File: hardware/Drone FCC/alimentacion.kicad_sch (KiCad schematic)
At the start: 20 parts, among them J901 PM02 PixHawk, Q901 Q_PMOS_GSD, U901 ZLDO1117QG33TA

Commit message: routing: connected everything
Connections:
- net 5V: now also C903.1, D902.1 (K), D903.1 (K), U901.3 (VI); no longer D903.2 (A), J901.1, J901.2
- net 5Vin: now also D903.2 (A), J901.1, J901.2; no longer C903.1, D902.1 (K), D903.1 (K), U901.3 (VI)
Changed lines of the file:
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@@
   (junction (at 42.545 133.35) (diameter 0) (color 0 0 0 0)
   )
+  (junction (at 174.625 36.195) (diameter 0) (color 0 0 0 0)
+  )
   (junction (at 167.64 36.195) (diameter 0) (color 0 0 0 0)
   )
@@
     (stroke (width 0) (type default) (color 0 0 0 0))
   )
-  (wire (pts (xy 167.64 36.195) (xy 182.245 36.195))
+  (wire (pts (xy 167.64 36.195) (xy 174.625 36.195))
     (stroke (width 0) (type default) (color 0 0 0 0))
   )
@@
     (stroke (width 0) (type default) (color 0 0 0 0))
   )
-  (wire (pts (xy 55.88 98.425) (xy 59.055 98.425))
+  (wire (pts (xy 55.88 98.425) (xy 60.325 98.425))
     (stroke (width 0) (type default) (color 0 0 0 0))
   )
@@
     (stroke (width 0) (type default) (color 0 0 0 0))
   )
+  (wire (pts (xy 174.625 27.305) (xy 174.625 36.195))
+    (stroke (width 0) (type default) (color 0 0 0 0))
+  )
   (wire (pts (xy 79.375 104.14) (xy 79.375 120.65))
     (stroke (width 0) (type default) (color 0 0 0 0))
@@
     (stroke (width 0) (type default) (color 0 0 0 0))
   )
+  (wire (pts (xy 179.705 27.305) (xy 174.625 27.305))
+    (stroke (width 0) (type default) (color 0 0 0 0))
+  )
   (wire (pts (xy 85.725 54.61) (xy 62.865 54.61))
     (stroke (width 0) (type default) (color 0 0 0 0))
@@
   )
   (wire (pts (xy 139.065 26.035) (xy 149.86 26.035))
+    (stroke (width 0) (type default) (color 0 0 0 0))
+  )
+  (wire (pts (xy 174.625 36.195) (xy 182.245 36.195))
     (stroke (width 0) (type default) (color 0 0 0 0))
   )
@@
     (effects (font (size 1.27 1.27)) (justify left bottom))
   )
-  (label "5Vin" (at 171.45 36.195 0)
-    (effects (font (size 1.27 1.27)) (justify left bottom))
-  )
-  (global_label "5V" (shape input) (at 137.795 52.07 180) (fields_autoplaced)
-    (effects (font (size 1.27 1.27)) (justify right))
-    (property "Intersheet References" "${INTERSHEET_REFS}" (id 0) (at 133.0838 52.1494 0)
-      (effects (font (size 1.27 1.27)) (justify right) hide)
-    )
+  (label "5Vin" (at 137.795 52.07 0)
+    (effects (font (size 1.27 1.27)) (justify left bottom))
+  )
+  (label "5Vin" (at 60.325 98.425 180)
+    (effects (font (size 1.27 1.27)) (justify right bottom))
   )
   (global_label "3V3" (shape input) (at 243.205 36.195 0) (fields_autoplaced)
@@
     )
   )
-  (global_label "5V" (shape input) (at 59.055 98.425 0) (fields_autoplaced)
+  (global_label "5V" (shape input) (at 179.705 27.305 0) (fields_autoplaced)
     (effects (font (size 1.27 1.27)) (justify left))
-    (property "Intersheet References" "${INTERSHEET_REFS}" (id 0) (at 63.7662 98.3456 0)
+    (property "Intersheet References" "${INTERSHEET_REFS}" (id 0) (at 184.4162 27.2256 0)
       (effects (font (size 1.27 1.27)) (justify left) hide)
     )

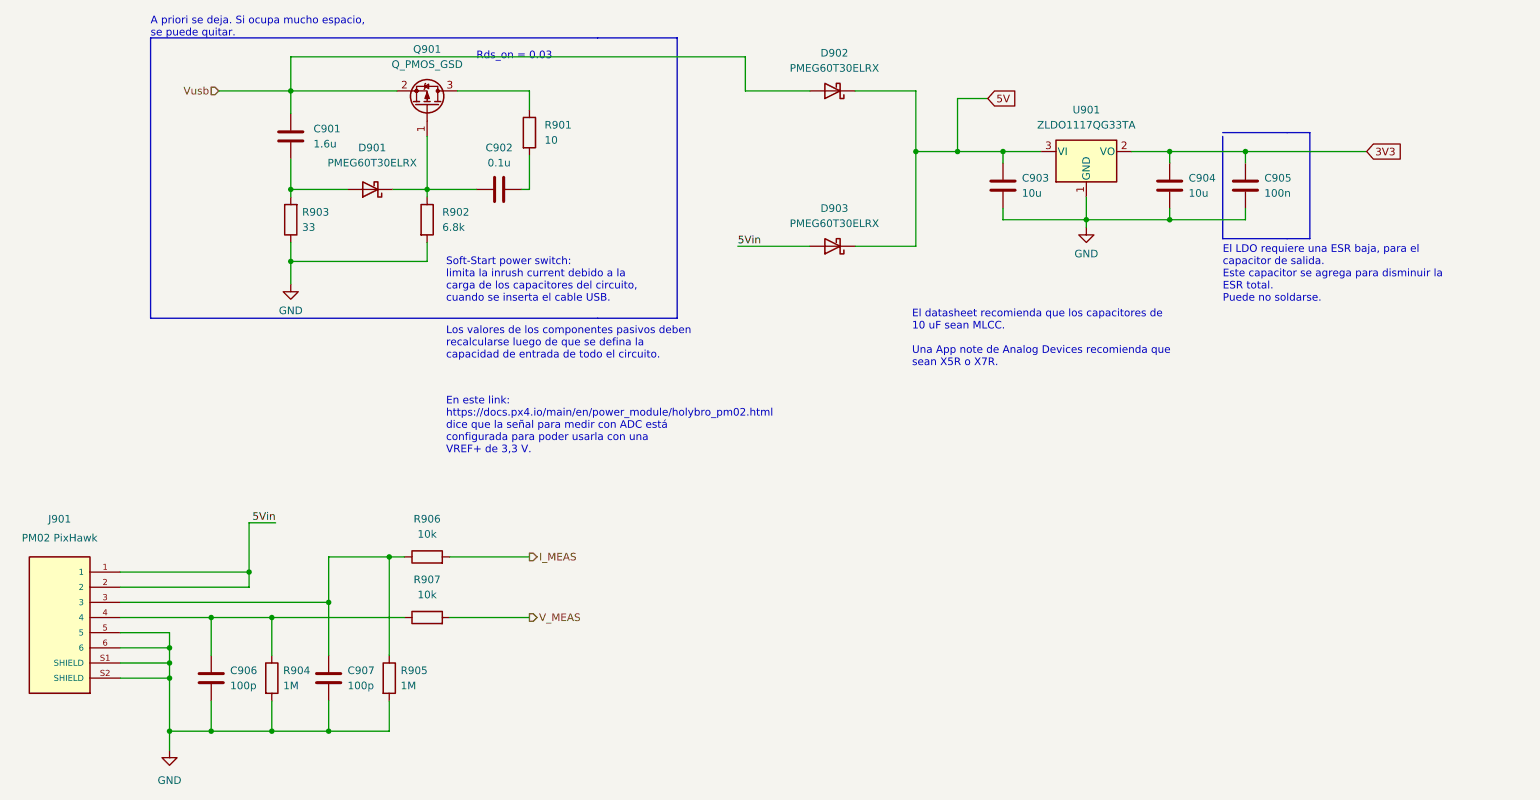
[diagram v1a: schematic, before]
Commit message: included all components on PCB
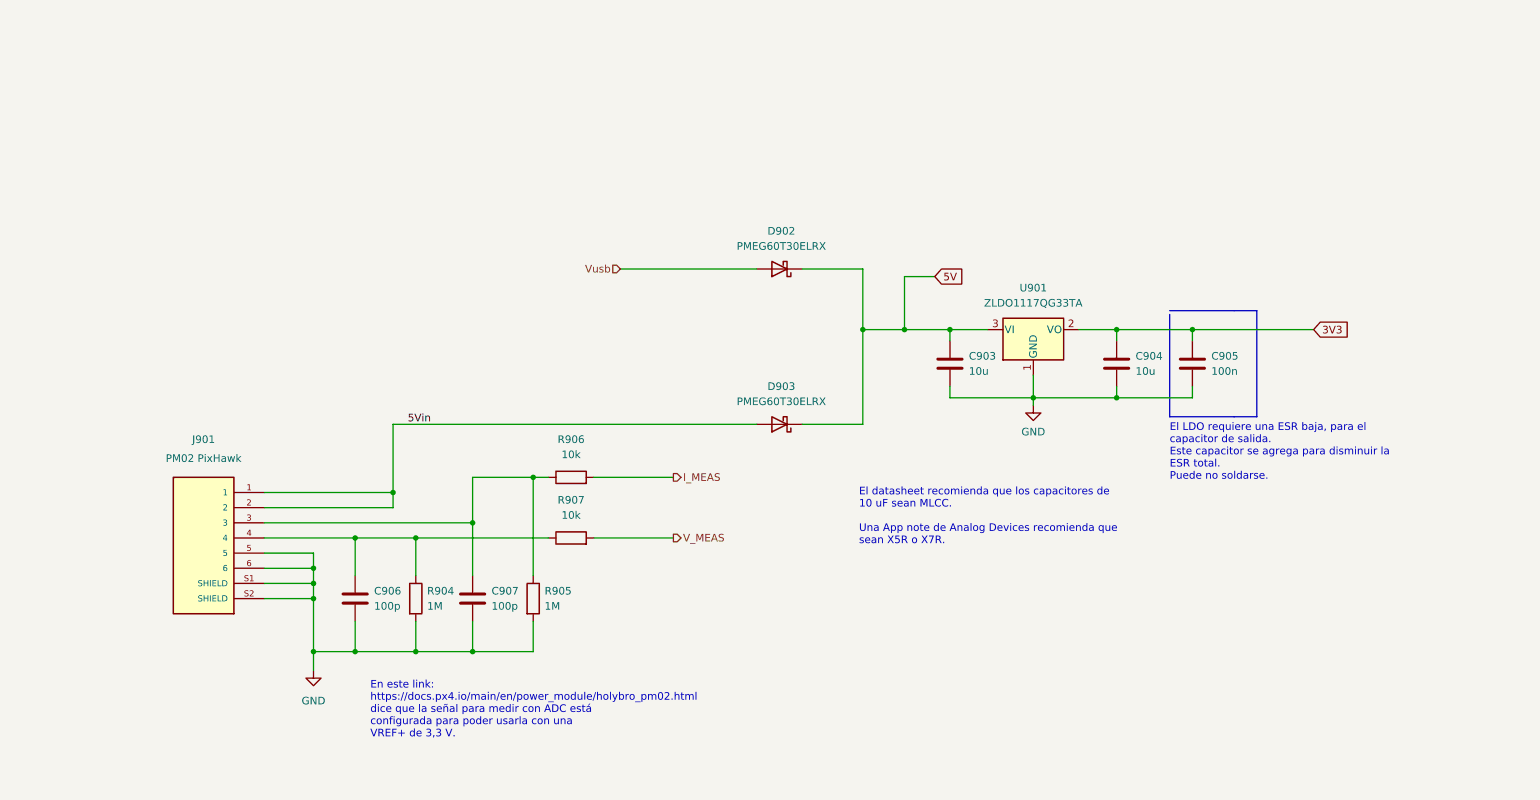
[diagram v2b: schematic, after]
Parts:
- removed C901: 1.6u, Capacitor_SMD:C_0603_1608Metric_Pad1.08x0.95mm_HandSolder, symbol Device:C
- removed C902: 0.1u, Capacitor_SMD:C_0603_1608Metric_Pad1.08x0.95mm_HandSolder, symbol Device:C
- removed D901: PMEG60T30ELRX, PMEG60T30ELRX:SODFL3517X110N, symbol Device:D_Schottky
- removed Q901: Q_PMOS_GSD, Package_TO_SOT_SMD:SOT-23, symbol Device:Q_PMOS_GSD
- removed R901: 10, Resistor_SMD:R_0603_1608Metric_Pad0.98x0.95mm_HandSolder, symbol Device:R
- removed R902: 6.8k, Resistor_SMD:R_0603_1608Metric_Pad0.98x0.95mm_HandSolder, symbol Device:R
- removed R903: 33, Resistor_SMD:R_0603_1608Metric_Pad0.98x0.95mm_HandSolder, symbol Device:R
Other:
- note removed: "A priori se deja. Si ocupa mucho espacio, se puede quitar."
- note removed: "Los valores de los componentes pasivos deben recalcularse luego de que se defina la capacidad de entrada de todo el circuito."
- note removed: "Rds_on = 0.03"
- note removed: "Soft-Start power switch: limita la inrush current debido a la carga de los capacitores del circuito, cuando se inserta el cable USB."
- moved on the sheet: C903, C904, C905, C906, C907, D902, D903, J901, R904, R905, R906, R907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

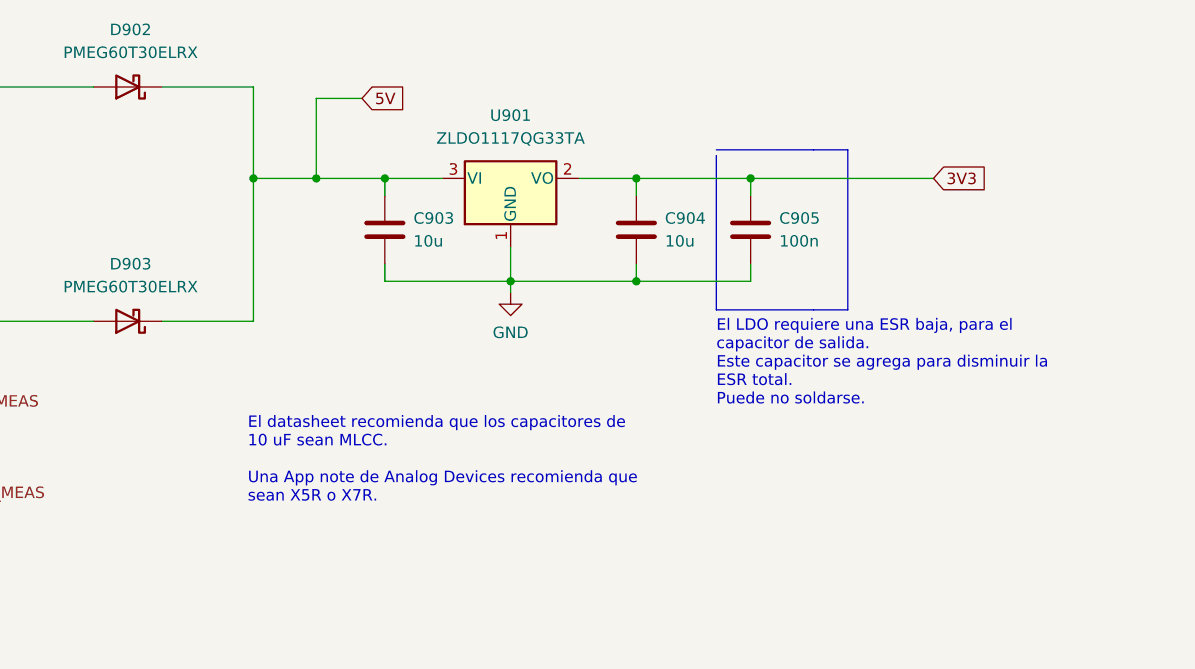
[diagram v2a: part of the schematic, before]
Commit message: LDO layout on PCB
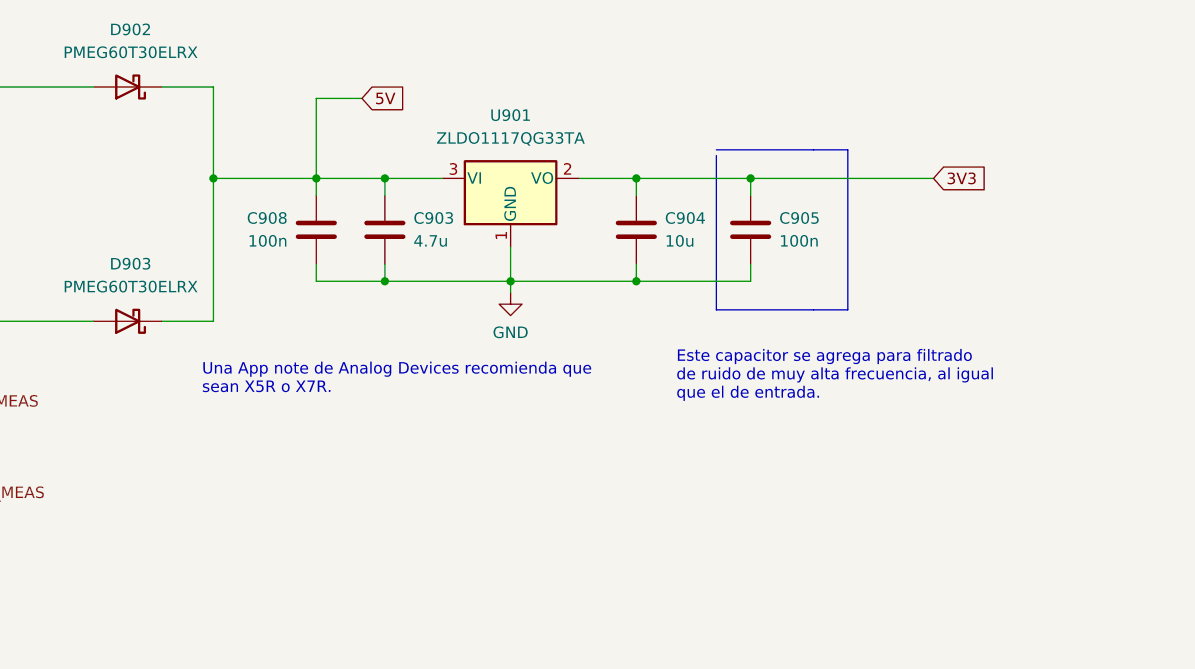
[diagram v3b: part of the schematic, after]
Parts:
- added C908: 100n, Capacitor_SMD:C_0603_1608Metric_Pad1.08x0.95mm_HandSolder, symbol Device:C
- C903: value 10u -> 4.7u; footprint Capacitor_SMD:C_0805_2012Metric_Pad1.18x1.45mm_HandSolder -> Capacitor_SMD:C_1206_3216Metric_Pad1.33x1.80mm_HandSolder
- C904: footprint Capacitor_SMD:C_0805_2012Metric_Pad1.18x1.45mm_HandSolder -> T491A106K016ATAUTO:CAPC3216X110N
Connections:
- net 5V: now also C908.2
- net GND: now also C908.1
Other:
- note added: "Este capacitor se agrega para filtrado de ruido de muy alta frecuencia, al igual que el de entrada."
- note added: "Una App note de Analog Devices recomienda que sean X5R o X7R."
- note removed: "El LDO requiere una ESR baja, para el capacitor de salida. Este capacitor se agrega para disminuir la ESR total. Puede no soldarse."
- note removed: "El datasheet recomienda que los capacitores de 10 uF sean MLCC. Una App note de Analog Devices recomienda que sean X5R o X7R."
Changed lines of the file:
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@@
   (junction (at 187.325 77.47) (diameter 0) (color 0 0 0 0)
   )
+  (junction (at 154.305 66.04) (diameter 0) (color 0 0 0 0)
+  )
   (junction (at 66.675 108.585) (diameter 0) (color 0 0 0 0)
   )
@@
   (junction (at 66.675 120.015) (diameter 0) (color 0 0 0 0)
   )
+  (junction (at 173.355 77.47) (diameter 0) (color 0 0 0 0)
+  )
   (junction (at 165.735 66.04) (diameter 0) (color 0 0 0 0)
   )
-  (junction (at 158.75 66.04) (diameter 0) (color 0 0 0 0)
-  )
   (junction (at 66.675 106.045) (diameter 0) (color 0 0 0 0)
   )
@@
     (stroke (width 0) (type default) (color 0 0 0 0))
   )
+  (wire (pts (xy 173.355 77.47) (xy 187.325 77.47))
+    (stroke (width 0) (type default) (color 0 0 0 0))
+  )
   (wire (pts (xy 66.675 103.505) (xy 66.675 106.045))
     (stroke (width 0) (type default) (color 0 0 0 0))
@@
     (stroke (width 0) (type default) (color 0 0 0 0))
   )
-  (wire (pts (xy 158.75 66.04) (xy 165.735 66.04))
+  (wire (pts (xy 154.305 66.04) (xy 165.735 66.04))
     (stroke (width 0) (type default) (color 0 0 0 0))
   )
@@
     (stroke (width 0) (type default) (color 0 0 0 0))
   )
-  (wire (pts (xy 148.59 81.915) (xy 158.75 81.915))
+  (wire (pts (xy 165.735 66.04) (xy 165.735 67.945))
+    (stroke (width 0) (type default) (color 0 0 0 0))
+  )
+  (wire (pts (xy 148.59 81.915) (xy 154.305 81.915))
     (stroke (width 0) (type default) (color 0 0 0 0))
   )
@@
     (stroke (width 0) (type default) (color 0 0 0 0))
   )
-  (wire (pts (xy 148.59 55.88) (xy 158.75 55.88))
+  (wire (pts (xy 148.59 55.88) (xy 154.305 55.88))
     (stroke (width 0) (type default) (color 0 0 0 0))
   )
@@
     (stroke (width 0) (type default) (color 0 0 0 0))
   )
-  (wire (pts (xy 158.75 66.04) (xy 158.75 81.915))
-    (stroke (width 0) (type default) (color 0 0 0 0))
-  )
-  (wire (pts (xy 158.75 55.88) (xy 158.75 66.04))
+  (wire (pts (xy 154.305 55.88) (xy 154.305 66.04))
     (stroke (width 0) (type default) (color 0 0 0 0))
   )
@@
     (stroke (width 0) (type default) (color 0 0 0 0))
   )
+  (wire (pts (xy 165.735 75.565) (xy 165.735 77.47))
+    (stroke (width 0) (type default) (color 0 0 0 0))
+  )
   (wire (pts (xy 66.675 106.045) (xy 66.675 108.585))
     (stroke (width 0) (type default) (color 0 0 0 0))
@@
     (stroke (width 0) (type default) (color 0 0 0 0))
   )
-  (wire (pts (xy 173.355 77.47) (xy 187.325 77.47))
+  (wire (pts (xy 165.735 77.47) (xy 173.355 77.47))
     (stroke (width 0) (type default) (color 0 0 0 0))
   )
@@
     (stroke (width 0) (type default) (color 0 0 0 0))
   )
+  (wire (pts (xy 154.305 66.04) (xy 154.305 81.915))
+    (stroke (width 0) (type default) (color 0 0 0 0))
+  )
   (wire (pts (xy 118.11 55.88) (xy 140.97 55.88))
     (stroke (width 0) (type default) (color 0 0 0 0))
@@
     (stroke (width 0) (type default) (color 0 0 0 0))
   )
-  (text "El LDO requiere una ESR baja, para el\ncapacitor de salida.\nEste capacitor se agrega para disminuir la \nESR total.\nPuede no soldarse."
-    (at 210.185 91.44 0)
+  (text "Este capacitor se agrega para filtrado\nde ruido de muy alta frecuencia, al igual\nque el de entrada."
+    (at 205.74 90.805 0)
     (effects (font (size 1.27 1.27)) (justify left bottom))
   )
@@
     (effects (font (size 1.27 1.27)) (justify left bottom))
   )
-  (text "El datasheet recomienda que los capacitores de\n10 uF sean MLCC.\n\nUna App note de Analog Devices recomienda que \nsean X5R o X7R."
-    (at 158.115 102.235 0)
+  (text "Una App note de Analog Devices recomienda que \nsean X5R o X7R."
+    (at 153.035 90.17 0)
     (effects (font (size 1.27 1.27)) (justify left bottom))
   )
@@
       (effects (font (size 1.27 1.27)) (justify right))
     )
-    (property "Value" "10u" (id 1) (at 176.53 73.0249 0)
+    (property "Value" "4.7u" (id 1) (at 176.53 73.0249 0)
       (effects (font (size 1.27 1.27)) (justify right))
     )
-    (property "Footprint" "Capacitor_SMD:C_0805_2012Metric_Pad1.18x1.45mm_HandSolder" (id 2) (at 172.3898 75.565 0)
+    (property "Footprint" "Capacitor_SMD:C_1206_3216Metric_Pad1.33x1.80mm_HandSolder" (id 2) (at 172.3898 75.565 0)
       (effects (font (size 1.27 1.27)) hide)
     )
@@
     (pin "2")
   )
+  (symbol (lib_id "Device:C") (at 165.735 71.755 0) (mirror x) (unit 1)
+    (in_bom yes) (on_board yes) (fields_autoplaced)
+    (property "Reference" "C908" (id 0) (at 162.56 70.4849 0)
+      (effects (font (size 1.27 1.27)) (justify right))
+    )
+    (property "Value" "100n" (id 1) (at 162.56 73.0249 0)
+      (effects (font (size 1.27 1.27)) (justify right))
+    )
+    (property "Footprint" "Capacitor_SMD:C_0603_1608Metric_Pad1.08x0.95mm_HandSolder" (id 2) (at 166.7002 67.945 0)
+      (effects (font (size 1.27 1.27)) hide)
+    )
+    (property "Datasheet" "~" (id 3) (at 165.735 71.755 0)
+      (effects (font (size 1.27 1.27)) hide)
+    )
+    (pin "1")
+    (pin "2")
+  )
   (symbol (lib_id "Device:C") (at 213.995 71.755 0) (unit 1)
     (in_bom yes) (on_board yes) (fields_autoplaced)
@@
       (effects (font (size 1.27 1.27)) (justify left))
     )
-    (property "Footprint" "Capacitor_SMD:C_0805_2012Metric_Pad1.18x1.45mm_HandSolder" (id 2) (at 202.2602 75.565 0)
-      (effects (font (size 1.27 1.27)) hide)
-    )
+    (property "Footprint" "T491A106K016ATAUTO:CAPC3216X110N" (id 2) (at 202.2602 75.565 0)
+      (effects (font (size 1.27 1.27)) hide)
+    )

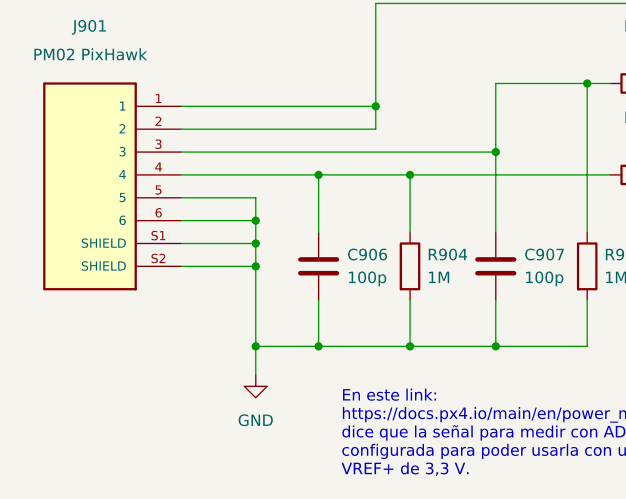
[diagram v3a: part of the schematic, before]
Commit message: add TVS diodes for SPI and ESD capacitors
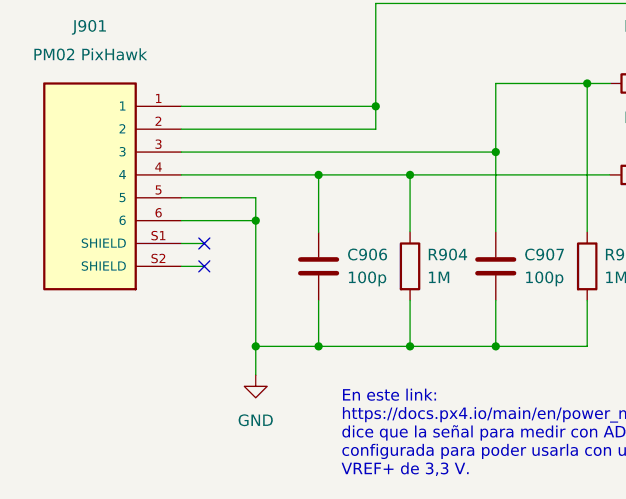
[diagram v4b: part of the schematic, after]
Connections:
- net GND: no longer J901.S1 (SHIELD), J901.S2 (SHIELD)
- no-connect marks 0 -> 2
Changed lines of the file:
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@@
   (junction (at 73.66 120.015) (diameter 0) (color 0 0 0 0)
   )
-  (junction (at 66.675 111.125) (diameter 0) (color 0 0 0 0)
-  )
   (junction (at 201.295 66.04) (diameter 0) (color 0 0 0 0)
   )
@@
   (junction (at 154.305 66.04) (diameter 0) (color 0 0 0 0)
   )
-  (junction (at 66.675 108.585) (diameter 0) (color 0 0 0 0)
-  )
   (junction (at 93.345 120.015) (diameter 0) (color 0 0 0 0)
   )
@@
   (junction (at 103.505 90.805) (diameter 0) (color 0 0 0 0)
   )
+  (no_connect (at 60.96 108.585))
+  (no_connect (at 60.96 111.125))
+  (wire (pts (xy 58.42 111.125) (xy 60.96 111.125))
+    (stroke (width 0) (type default) (color 0 0 0 0))
+  )
   (wire (pts (xy 187.325 77.47) (xy 201.295 77.47))
     (stroke (width 0) (type default) (color 0 0 0 0))
@@
     (stroke (width 0) (type default) (color 0 0 0 0))
   )
-  (wire (pts (xy 66.675 108.585) (xy 66.675 111.125))
-    (stroke (width 0) (type default) (color 0 0 0 0))
-  )
   (wire (pts (xy 173.355 77.47) (xy 187.325 77.47))
     (stroke (width 0) (type default) (color 0 0 0 0))
@@
     (stroke (width 0) (type default) (color 0 0 0 0))
   )
-  (wire (pts (xy 58.42 108.585) (xy 66.675 108.585))
+  (wire (pts (xy 58.42 108.585) (xy 60.96 108.585))
     (stroke (width 0) (type default) (color 0 0 0 0))
   )
@@
     (stroke (width 0) (type default) (color 0 0 0 0))
   )
-  (wire (pts (xy 66.675 111.125) (xy 66.675 120.015))
-    (stroke (width 0) (type default) (color 0 0 0 0))
-  )
   (wire (pts (xy 80.01 93.345) (xy 80.01 95.885))
     (stroke (width 0) (type default) (color 0 0 0 0))
@@
     (stroke (width 0) (type default) (color 0 0 0 0))
   )
-  (wire (pts (xy 66.675 106.045) (xy 66.675 108.585))
+  (wire (pts (xy 66.675 106.045) (xy 66.675 120.015))
     (stroke (width 0) (type default) (color 0 0 0 0))
   )
@@
     (stroke (width 0) (type default) (color 0 0 0 0))
   )
-  (wire (pts (xy 58.42 111.125) (xy 66.675 111.125))
-    (stroke (width 0) (type default) (color 0 0 0 0))
-  )
